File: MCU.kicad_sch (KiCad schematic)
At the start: 35 parts, among them J1 FTSH-105-01-L-DV-K-A, U1 EFR32FG23L020F128GM40-C, U2 Si7021-A20, Y1 39MHz 10pF

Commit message: completed layout and routing with preliminary matching network
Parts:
- renumbered C29 to C11, C11 to C12, C12 to C13, C13 to C14, C14 to C15, C15 to C16, C16 to C17, C17 to C18, C18 to C19
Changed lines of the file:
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@@
 		(dnp no)
 		(fields_autoplaced yes)
-		(property "Reference" "C18"
+		(property "Reference" "C19"
 			(at 210.82 88.8999 0)
 			(show_name no)
@@
 			(project "WINLAB-LP-Radio-Sensor-Hub"
 				(path "/0de7ee4a-bb98-4bc6-bb89-3afafc4b94b5/f02c211f-c559-4db5-8225-ca108efc3892"
-					(reference "C18")
+					(reference "C19")
 					(unit 1)
 				)
@@
 		(dnp no)
 		(fields_autoplaced yes)
-		(property "Reference" "C13"
+		(property "Reference" "C14"
 			(at 198.12 66.0399 0)
 			(show_name no)
@@
 			(project "WINLAB-LP-Radio-Sensor-Hub"
 				(path "/0de7ee4a-bb98-4bc6-bb89-3afafc4b94b5/f02c211f-c559-4db5-8225-ca108efc3892"
-					(reference "C13")
+					(reference "C14")
 					(unit 1)
 				)
@@
 		(dnp no)
 		(fields_autoplaced yes)
-		(property "Reference" "C12"
+		(property "Reference" "C13"
 			(at 184.15 96.5199 0)
 			(show_name no)
@@
 			(project "WINLAB-LP-Radio-Sensor-Hub"
 				(path "/0de7ee4a-bb98-4bc6-bb89-3afafc4b94b5/f02c211f-c559-4db5-8225-ca108efc3892"
-					(reference "C12")
+					(reference "C13")
 					(unit 1)
 				)
@@
 		(dnp no)
 		(fields_autoplaced yes)
-		(property "Reference" "C16"
+		(property "Reference" "C17"
 			(at 210.82 66.0399 0)
 			(show_name no)
@@
 			(project "WINLAB-LP-Radio-Sensor-Hub"
 				(path "/0de7ee4a-bb98-4bc6-bb89-3afafc4b94b5/f02c211f-c559-4db5-8225-ca108efc3892"
-					(reference "C16")
+					(reference "C17")
 					(unit 1)
 				)
@@
 		(dnp no)
 		(fields_autoplaced yes)
-		(property "Reference" "#PWR042"
+		(property "Reference" "#PWR013"
 			(at 160.02 173.99 0)
 			(hide yes)
@@
 			(project "WINLAB-LP-Radio-Sensor-Hub"
 				(path "/0de7ee4a-bb98-4bc6-bb89-3afafc4b94b5/f02c211f-c559-4db5-8225-ca108efc3892"
-					(reference "#PWR042")
+					(reference "#PWR013")
 					(unit 1)
 				)
@@
 		(dnp no)
 		(fields_autoplaced yes)
-		(property "Reference" "#PWR012"
+		(property "Reference" "#PWR016"
 			(at 219.71 64.77 0)
 			(hide yes)
@@
 			(project "WINLAB-LP-Radio-Sensor-Hub"
 				(path "/0de7ee4a-bb98-4bc6-bb89-3afafc4b94b5/f02c211f-c559-4db5-8225-ca108efc3892"
-					(reference "#PWR012")
+					(reference "#PWR016")
 					(unit 1)
 				)
@@
 		(dnp no)
 		(fields_autoplaced yes)
-		(property "Reference" "C17"
+		(property "Reference" "C18"
 			(at 210.82 77.4699 0)
 			(show_name no)
@@
 			(project "WINLAB-LP-Radio-Sensor-Hub"
 				(path "/0de7ee4a-bb98-4bc6-bb89-3afafc4b94b5/f02c211f-c559-4db5-8225-ca108efc3892"
-					(reference "C17")
+					(reference "C18")
 					(unit 1)
 				)
@@
 		(dnp no)
 		(fields_autoplaced yes)
-		(property "Reference" "C11"
+		(property "Reference" "C12"
 			(at 171.45 96.5199 0)
 			(show_name no)
@@
 			(project "WINLAB-LP-Radio-Sensor-Hub"
 				(path "/0de7ee4a-bb98-4bc6-bb89-3afafc4b94b5/f02c211f-c559-4db5-8225-ca108efc3892"
-					(reference "C11")
+					(reference "C12")
 					(unit 1)
 				)
@@
 		(dnp no)
 		(fields_autoplaced yes)
-		(property "Reference" "#PWR014"
+		(property "Reference" "#PWR018"
 			(at 270.51 130.81 0)
 			(hide yes)
@@
 			(project "WINLAB-LP-Radio-Sensor-Hub"
 				(path "/0de7ee4a-bb98-4bc6-bb89-3afafc4b94b5/f02c211f-c559-4db5-8225-ca108efc3892"
-					(reference "#PWR014")
+					(reference "#PWR018")
 					(unit 1)
 				)
@@
 		(dnp no)
 		(fields_autoplaced yes)
-		(property "Reference" "C14"
+		(property "Reference" "C15"
 			(at 198.12 77.4699 0)
 			(show_name no)
@@
 			(project "WINLAB-LP-Radio-Sensor-Hub"
 				(path "/0de7ee4a-bb98-4bc6-bb89-3afafc4b94b5/f02c211f-c559-4db5-8225-ca108efc3892"
-					(reference "C14")
+					(reference "C15")
 					(unit 1)
 				)
@@
 		(dnp no)
 		(fields_autoplaced yes)
-		(property "Reference" "#PWR013"
+		(property "Reference" "#PWR017"
 			(at 219.71 157.48 0)
 			(hide yes)
@@
 			(project "WINLAB-LP-Radio-Sensor-Hub"
 				(path "/0de7ee4a-bb98-4bc6-bb89-3afafc4b94b5/f02c211f-c559-4db5-8225-ca108efc3892"
-					(reference "#PWR013")
+					(reference "#PWR017")
 					(unit 1)
 				)
@@
 		(dnp no)
 		(fields_autoplaced yes)
-		(property "Reference" "#PWR011"
+		(property "Reference" "#PWR015"
 			(at 217.17 106.68 0)
 			(hide yes)
@@
 			(project "WINLAB-LP-Radio-Sensor-Hub"
 				(path "/0de7ee4a-bb98-4bc6-bb89-3afafc4b94b5/f02c211f-c559-4db5-8225-ca108efc3892"
-					(reference "#PWR011")
+					(reference "#PWR015")
 					(unit 1)
 				)
@@
 		(dnp no)
 		(fields_autoplaced yes)
-		(property "Reference" "#PWR044"
+		(property "Reference" "#PWR012"
 			(at 156.21 59.69 0)
 			(hide yes)
@@
 			(project "WINLAB-LP-Radio-Sensor-Hub"
 				(path "/0de7ee4a-bb98-4bc6-bb89-3afafc4b94b5/f02c211f-c559-4db5-8225-ca108efc3892"
-					(reference "#PWR044")
+					(reference "#PWR012")
 					(unit 1)
 				)
@@
 		(dnp no)
 		(fields_autoplaced yes)
-		(property "Reference" "#PWR041"
+		(property "Reference" "#PWR011"
 			(at 144.78 168.91 0)
 			(hide yes)
@@
 			(project "WINLAB-LP-Radio-Sensor-Hub"
 				(path "/0de7ee4a-bb98-4bc6-bb89-3afafc4b94b5/f02c211f-c559-4db5-8225-ca108efc3892"
-					(reference "#PWR041")
+					(reference "#PWR011")
 					(unit 1)
 				)
@@
 		(dnp no)
 		(fields_autoplaced yes)
-		(property "Reference" "C15"
+		(property "Reference" "C16"
 			(at 198.12 88.8999 0)
 			(show_name no)
@@
 			(project "WINLAB-LP-Radio-Sensor-Hub"
 				(path "/0de7ee4a-bb98-4bc6-bb89-3afafc4b94b5/f02c211f-c559-4db5-8225-ca108efc3892"
-					(reference "C15")
+					(reference "C16")
 					(unit 1)
 				)
@@
 		(dnp no)
 		(fields_autoplaced yes)
-		(property "Reference" "#PWR010"
+		(property "Reference" "#PWR014"
 			(at 180.34 71.12 0)
 			(hide yes)
@@
 			(project "WINLAB-LP-Radio-Sensor-Hub"
 				(path "/0de7ee4a-bb98-4bc6-bb89-3afafc4b94b5/f02c211f-c559-4db5-8225-ca108efc3892"
-					(reference "#PWR010")
+					(reference "#PWR014")
 					(unit 1)
 				)
@@
 		(dnp no)
 		(fields_autoplaced yes)
-		(property "Reference" "#PWR043"
+		(property "Reference" "#PWR010"
 			(at 142.24 196.85 0)
 			(hide yes)
@@
 			(project "WINLAB-LP-Radio-Sensor-Hub"
 				(path "/0de7ee4a-bb98-4bc6-bb89-3afafc4b94b5/f02c211f-c559-4db5-8225-ca108efc3892"
-					(reference "#PWR043")
+					(reference "#PWR010")
 					(unit 1)
 				)
@@
 		(dnp no)
 		(fields_autoplaced yes)
-		(property "Reference" "C29"
+		(property "Reference" "C11"
 			(at 153.67 158.75 90)
 			(show_name no)
@@
 			(project "WINLAB-LP-Radio-Sensor-Hub"
 				(path "/0de7ee4a-bb98-4bc6-bb89-3afafc4b94b5/f02c211f-c559-4db5-8225-ca108efc3892"
-					(reference "C29")
+					(reference "C11")
 					(unit 1)
 				)

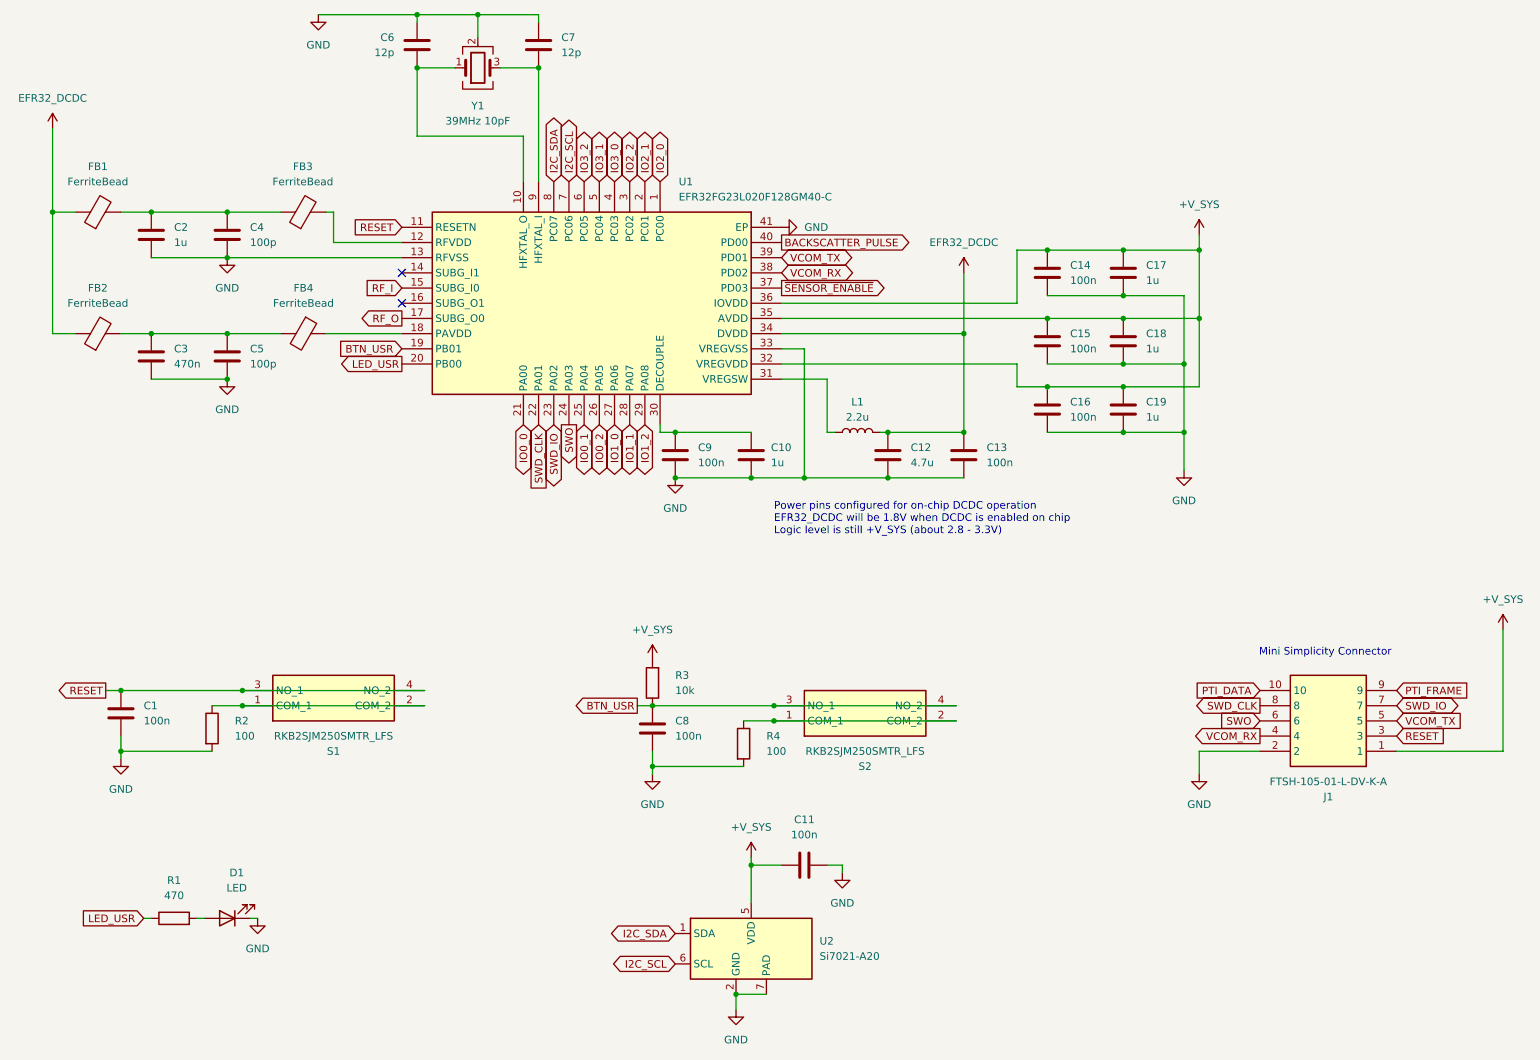
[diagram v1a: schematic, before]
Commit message: USB charging, UVP HW supervisor, PAVDD selection, charger IC enable jumper, layout and silkscreen changes
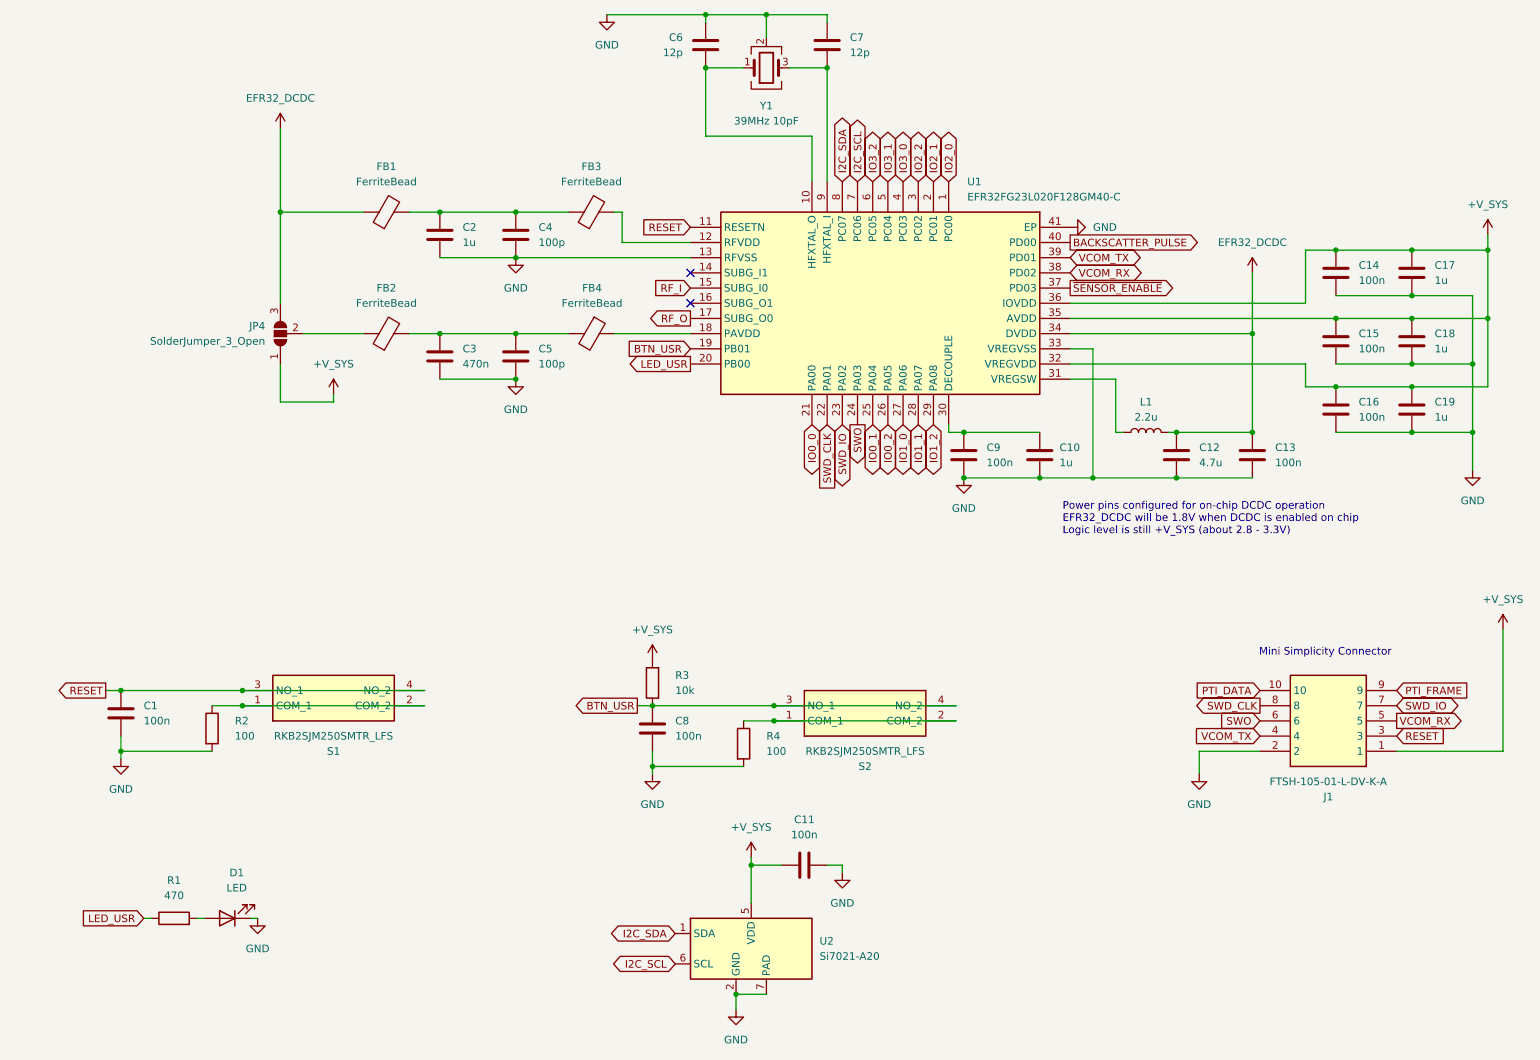
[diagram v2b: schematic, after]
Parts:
- added JP4: SolderJumper_3_Open, Jumper:SolderJumper-3_P1.3mm_Open_RoundedPad1.0x1.5mm, symbol Jumper:SolderJumper_3_Open
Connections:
- net +V_SYS: now also JP4.1 (A)
- net EFR32_DCDC: now also JP4.3 (B); no longer FB2.1
- net VCOM_RX: now also J1.5; no longer J1.4
- net VCOM_TX: now also J1.4; no longer J1.5
- new net: FB2.1, JP4.2 (C)
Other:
- moved on the sheet: C10, C12, C13, C14, C15, C16, C17, C18, C19, C2, C3, C4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
